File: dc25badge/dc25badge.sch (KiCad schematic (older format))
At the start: 34 parts, among them P1 BATT, P2 USB_OTG, P3 CORTEX, SW1 RESET, SW3 MODE, SW4 BRIGHT, U1 MIC5305, U2 TPS61232, U3 ATSAMD21E18A-AU, U4 74AHCT125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

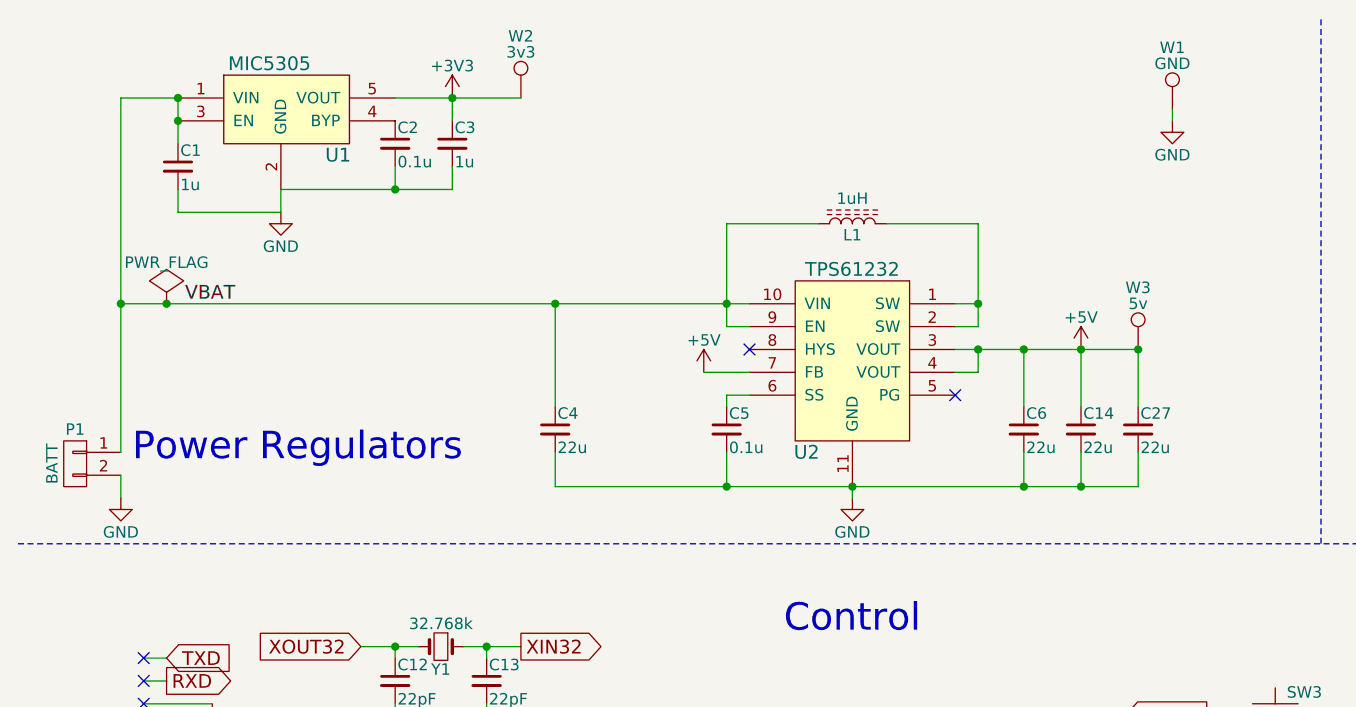
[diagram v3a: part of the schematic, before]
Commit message: Add reverse polarity MOSFET.
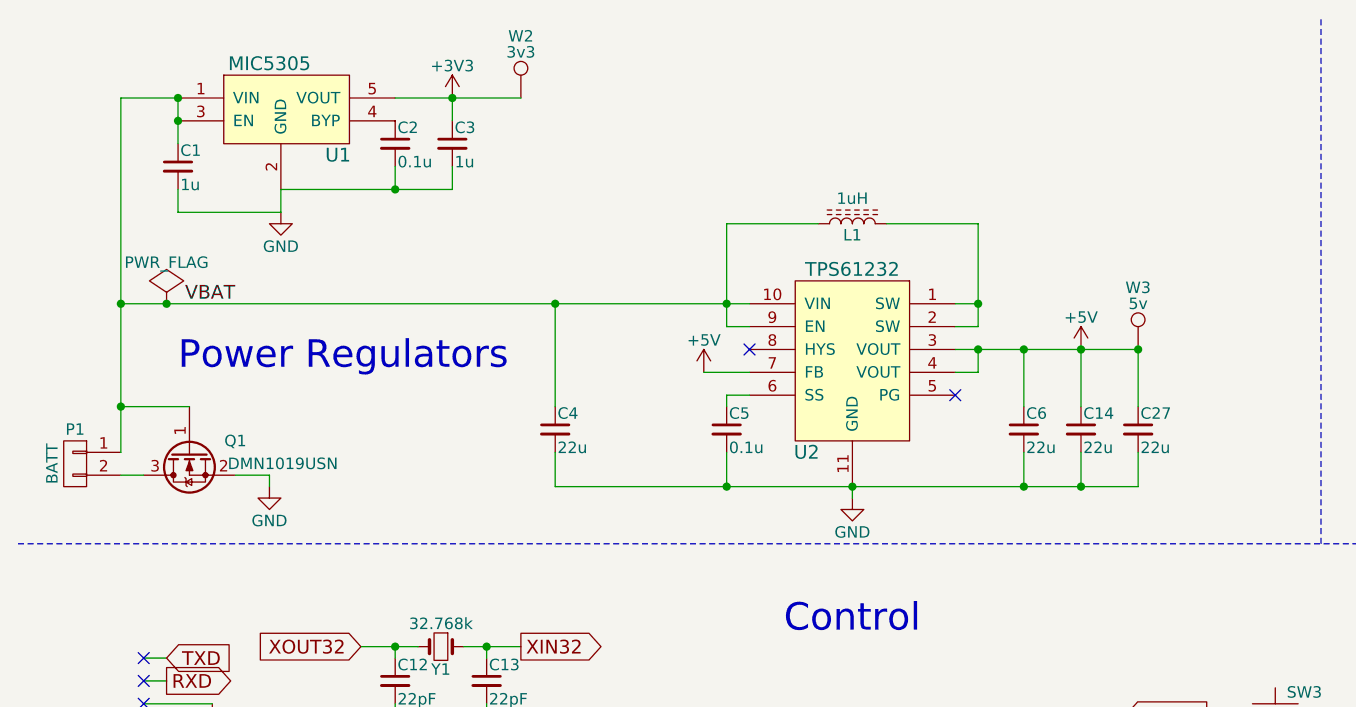
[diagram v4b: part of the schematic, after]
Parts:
- removed W1: GND, Measurement_Points:Measurement_Point_Round-SMD-Pad_Big, symbol TEST_1P
- added Q1: DMN1019USN, TO_SOT_Packages_SMD:SOT-23, symbol Q_NMOS_GSD
- C1, C10, C11, C14, C2, C27, C3, C4, C5, C6, C7, C8, C9: footprint Capacitors_SMD:C_0805_HandSoldering -> Capacitors_SMD:C_0805
- C12, C13: footprint Capacitors_SMD:C_0603_HandSoldering -> Capacitors_SMD:C_0603
- R1, R5, R6: footprint Resistors_SMD:R_0805_HandSoldering -> Resistors_SMD:R_0805
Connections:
- net GND: now also Q1.2 (S); no longer P1.2 (P2)
- net VBAT: now also Q1.1 (G)
- new net: P1.2 (P2), Q1.3 (D)
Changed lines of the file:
@@
 F 0 "C2" H 2160 1120 50  0000 L CNN
 F 1 "0.1u" H 2160 970 50  0000 L CNN
-F 2 "Capacitors_SMD:C_0805_HandSoldering" H 2150 1050 50  0001 C CNN
+F 2 "Capacitors_SMD:C_0805" H 2150 1050 50  0001 C CNN
 F 3 "" H 2150 1050 50  0000 C CNN
 	1    2150 1050
@@
 F 0 "C1" H 1210 1220 50  0000 L CNN
 F 1 "1u" H 1210 1070 50  0000 L CNN
-F 2 "Capacitors_SMD:C_0805_HandSoldering" H 1200 1150 50  0001 C CNN
+F 2 "Capacitors_SMD:C_0805" H 1200 1150 50  0001 C CNN
 F 3 "" H 1200 1150 50  0000 C CNN
 	1    1200 1150
@@
 F 0 "C3" H 2410 1120 50  0000 L CNN
 F 1 "1u" H 2410 970 50  0000 L CNN
-F 2 "Capacitors_SMD:C_0805_HandSoldering" H 2400 1050 50  0001 C CNN
+F 2 "Capacitors_SMD:C_0805" H 2400 1050 50  0001 C CNN
 F 3 "" H 2400 1050 50  0000 C CNN
 	1    2400 1050
@@
 L GND #PWR02
 U 1 1 592A5659
-P 950 2600
-F 0 "#PWR02" H 950 2350 50  0001 C CNN
-F 1 "GND" H 950 2450 50  0000 C CNN
-F 2 "" H 950 2600 50  0000 C CNN
-F 3 "" H 950 2600 50  0000 C CNN
-	1    950  2600
+P 1600 2550
+F 0 "#PWR02" H 1600 2300 50  0001 C CNN
+F 1 "GND" H 1600 2400 50  0000 C CNN
+F 2 "" H 1600 2550 50  0000 C CNN
+F 3 "" H 1600 2550 50  0000 C CNN
+	1    1600 2550
 	1    0    0    -1
 $EndComp
@@
 	1    0    0    -1
 $EndComp
-Text Notes 1000 2450 0    120  ~ 0
+Text Notes 1200 2050 0    120  ~ 0
 Power Regulators
 $Comp
@@
 F 0 "C7" H 1410 5620 50  0000 L CNN
 F 1 "0.1u" H 1410 5470 50  0000 L CNN
-F 2 "Capacitors_SMD:C_0805_HandSoldering" H 1400 5550 50  0001 C CNN
+F 2 "Capacitors_SMD:C_0805" H 1400 5550 50  0001 C CNN
 F 3 "" H 1400 5550 50  0000 C CNN
 	1    1400 5550
@@
 F 0 "C9" H 3960 5620 50  0000 L CNN
 F 1 "0.1u" H 3960 5470 50  0000 L CNN
-F 2 "Capacitors_SMD:C_0805_HandSoldering" H 3950 5550 50  0001 C CNN
+F 2 "Capacitors_SMD:C_0805" H 3950 5550 50  0001 C CNN
 F 3 "" H 3950 5550 50  0000 C CNN
 	1    3950 5550
@@
 F 0 "C10" H 4210 5620 50  0000 L CNN
 F 1 "0.1u" H 4210 5470 50  0000 L CNN
-F 2 "Capacitors_SMD:C_0805_HandSoldering" H 4200 5550 50  0001 C CNN
+F 2 "Capacitors_SMD:C_0805" H 4200 5550 50  0001 C CNN
 F 3 "" H 4200 5550 50  0000 C CNN
 	1    4200 5550
@@
 F 0 "R6" H 1680 6320 50  0000 L CNN
 F 1 "10k" H 1680 6260 50  0000 L CNN
-F 2 "Resistors_SMD:R_0805_HandSoldering" H 1650 6300 50  0001 C CNN
+F 2 "Resistors_SMD:R_0805" H 1650 6300 50  0001 C CNN
 F 3 "" H 1650 6300 50  0000 C CNN
 	1    1650 6300
@@
 F 0 "C11" H 4460 5620 50  0000 L CNN
 F 1 "10u" H 4460 5470 50  0000 L CNN
-F 2 "Capacitors_SMD:C_0805_HandSoldering" H 4450 5550 50  0001 C CNN
+F 2 "Capacitors_SMD:C_0805" H 4450 5550 50  0001 C CNN
 F 3 "" H 4450 5550 50  0000 C CNN
 	1    4450 5550
@@
 F 0 "C8" H 1660 6870 50  0000 L CNN
 F 1 "0.1u" H 1660 6720 50  0000 L CNN
-F 2 "Capacitors_SMD:C_0805_HandSoldering" H 1650 6800 50  0001 C CNN
+F 2 "Capacitors_SMD:C_0805" H 1650 6800 50  0001 C CNN
 F 3 "" H 1650 6800 50  0000 C CNN
 	1    1650 6800
@@
 F 0 "R5" H 1430 6620 50  0000 L CNN
 F 1 "330" H 1430 6560 50  0000 L CNN
-F 2 "Resistors_SMD:R_0805_HandSoldering" H 1400 6600 50  0001 C CNN
+F 2 "Resistors_SMD:R_0805" H 1400 6600 50  0001 C CNN
 F 3 "" H 1400 6600 50  0000 C CNN
 	1    1400 6600
@@
 	1    0    0    -1
 $EndComp
-$Comp
-L TEST_1P W1
-U 1 1 592AB837
-P 5550 900
-F 0 "W1" H 5550 1170 50  0000 C CNN
-F 1 "GND" H 5550 1100 50  0000 C CNN
-F 2 "Measurement_Points:Measurement_Point_Round-SMD-Pad_Big" H 5750 900 50  0001 C CNN
-F 3 "" H 5750 900 50  0000 C CNN
-	1    5550 900
-	1    0    0    -1
-$EndComp
 Text GLabel 7200 4600 2    60   Output ~ 0
 SPI_CLK
 Text GLabel 7200 5300 2    60   Output ~ 0
 SPI_MOSI
-$Comp
-L GND #PWR015
-U 1 1 592ACB78
-P 5550 950
-F 0 "#PWR015" H 5550 700 50  0001 C CNN
-F 1 "GND" H 5550 800 50  0000 C CNN
-F 2 "" H 5550 950 50  0000 C CNN
-F 3 "" H 5550 950 50  0000 C CNN
-	1    5550 950
-	1    0    0    -1
-$EndComp
 Wire Wire Line
 	2400 1250 2400 1150
@@
 F 0 "C13" H 2560 3470 50  0000 L CNN
 F 1 "22pF" H 2560 3320 50  0000 L CNN
-F 2 "Capacitors_SMD:C_0603_HandSoldering" H 2550 3400 50  0001 C CNN
+F 2 "Capacitors_SMD:C_0603" H 2550 3400 50  0001 C CNN
 F 3 "" H 2550 3400 50  0000 C CNN
 	1    2550 3400
@@
 F 0 "C12" H 2160 3470 50  0000 L CNN
 F 1 "22pF" H 2160 3320 50  0000 L CNN
-F 2 "Capacitors_SMD:C_0603_HandSoldering" H 2150 3400 50  0001 C CNN
+F 2 "Capacitors_SMD:C_0603" H 2150 3400 50  0001 C CNN
 F 3 "" H 2150 3400 50  0000 C CNN
 	1    2150 3400
@@
 	6300 3800 6200 3800
 Connection ~ 6300 3800
-Wire Wire Line
-	950  2600 950  2500
 $Comp
 L TPS61232 U2
@@
 F 0 "C5" H 3610 2370 50  0000 L CNN
 F 1 "0.1u" H 3610 2220 50  0000 L CNN
-F 2 "Capacitors_SMD:C_0805_HandSoldering" H 3600 2300 50  0001 C CNN
+F 2 "Capacitors_SMD:C_0805" H 3600 2300 50  0001 C CNN
 F 3 "" H 3600 2300 50  0000 C CNN
 	1    3600 2300
@@
 F 0 "C4" H 2860 2370 50  0000 L CNN
 F 1 "22u" H 2860 2220 50  0000 L CNN
-F 2 "Capacitors_SMD:C_0805_HandSoldering" H 2850 2300 50  0001 C CNN
+F 2 "Capacitors_SMD:C_0805" H 2850 2300 50  0001 C CNN
 F 3 "" H 2850 2300 50  0000 C CNN
 	1    2850 2300
@@
 F 0 "C6" H 4910 2370 50  0000 L CNN
 F 1 "22u" H 4910 2220 50  0000 L CNN
-F 2 "Capacitors_SMD:C_0805_HandSoldering" H 4900 2300 50  0001 C CNN
+F 2 "Capacitors_SMD:C_0805" H 4900 2300 50  0001 C CNN
 F 3 "" H 4900 2300 50  0000 C CNN
 	1    4900 2300
@@
 F 0 "C14" H 5160 2370 50  0000 L CNN
 F 1 "22u" H 5160 2220 50  0000 L CNN
-F 2 "Capacitors_SMD:C_0805_HandSoldering" H 5150 2300 50  0001 C CNN
+F 2 "Capacitors_SMD:C_0805" H 5150 2300 50  0001 C CNN
 F 3 "" H 5150 2300 50  0000 C CNN
 	1    5150 2300
@@
 F 0 "C27" H 5410 2370 50  0000 L CNN
 F 1 "22u" H 5410 2220 50  0000 L CNN
-F 2 "Capacitors_SMD:C_0805_HandSoldering" H 5400 2300 50  0001 C CNN
+F 2 "Capacitors_SMD:C_0805" H 5400 2300 50  0001 C CNN
 F 3 "" H 5400 2300 50  0000 C CNN
 	1    5400 2300
@@
 Wire Wire Line
 	850  4400 850  4350
-Wire Wire Line
-	5550 900  5550 950
 NoConn ~ 3650 4250
 Wire Wire Line
@@
 F 0 "R1" H 6330 6170 50  0000 L CNN
 F 1 "330" H 6330 6110 50  0000 L CNN
-F 2 "Resistors_SMD:R_0805_HandSoldering" H 6300 6150 50  0001 C CNN
+F 2 "Resistors_SMD:R_0805" H 6300 6150 50  0001 C CNN
 F 3 "" H 6300 6150 50  0000 C CNN
 	1    6300 6150
@@
 Wire Wire Line
 	6850 6150 6850 6250
+$Comp
+L Q_NMOS_GSD Q1
+U 1 1 5939E8DA
+P 1250 2400
+F 0 "Q1" V 1200 2150 50  0000 L CNN
+F 1 "DMN1019USN" V 1300 1750 50  0000 L CNN
+F 2 "TO_SOT_Packages_SMD:SOT-23" H 1450 2500 50  0001 C CNN
+F 3 "" H 1250 2400 50  0000 C CNN
+	1    1250 2400
+	0    -1   1    0
+$EndComp
+Wire Wire Line
+	950  2500 1050 2500
+Wire Wire Line
+	1600 2550 1600 2500
+Wire Wire Line
+	1600 2500 1450 2500
+Wire Wire Line
+	1250 2200 950  2200
+Connection ~ 950  2200
 $EndSCHEMATC
